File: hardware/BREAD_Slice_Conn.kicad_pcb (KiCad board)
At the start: 2 copper layers, 70 x 100 mm, 15 parts, among them J1 Conn_01x10_Female

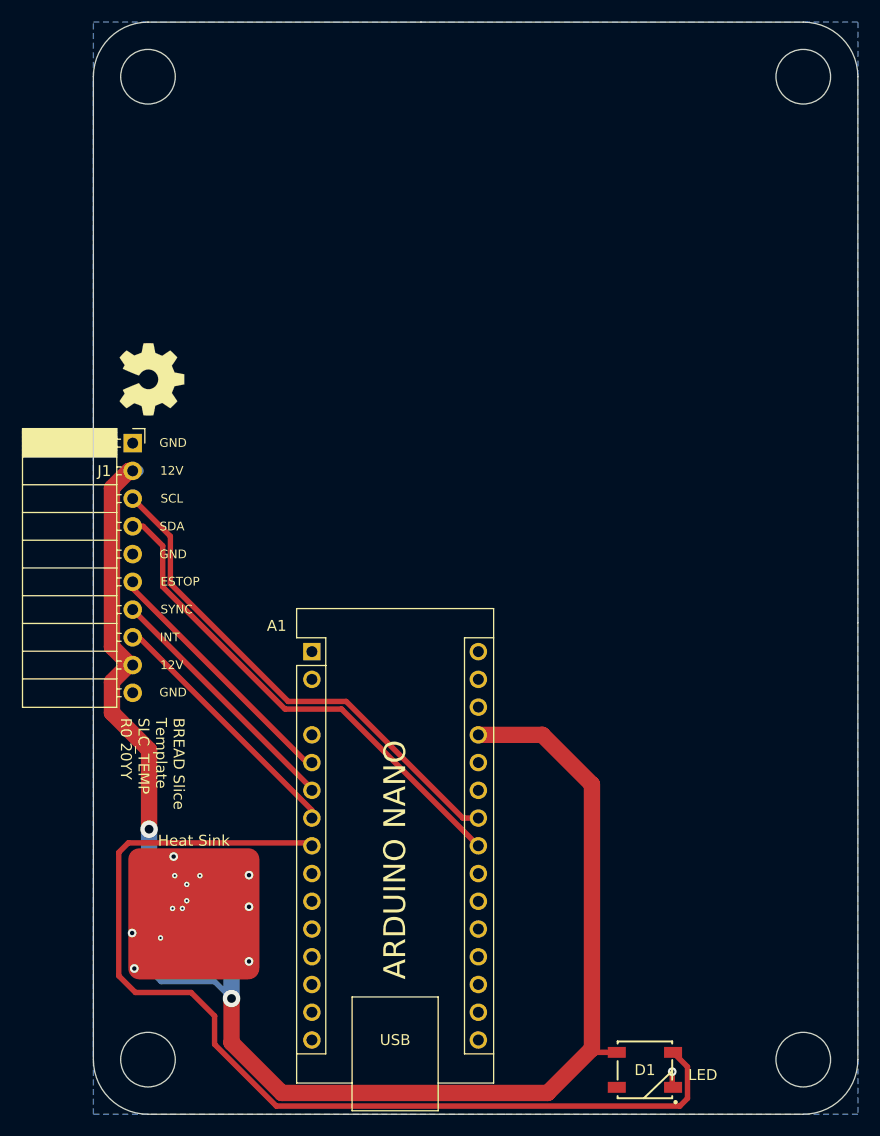
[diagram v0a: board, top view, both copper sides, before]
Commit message: updated template and added pcb vars for prototyping
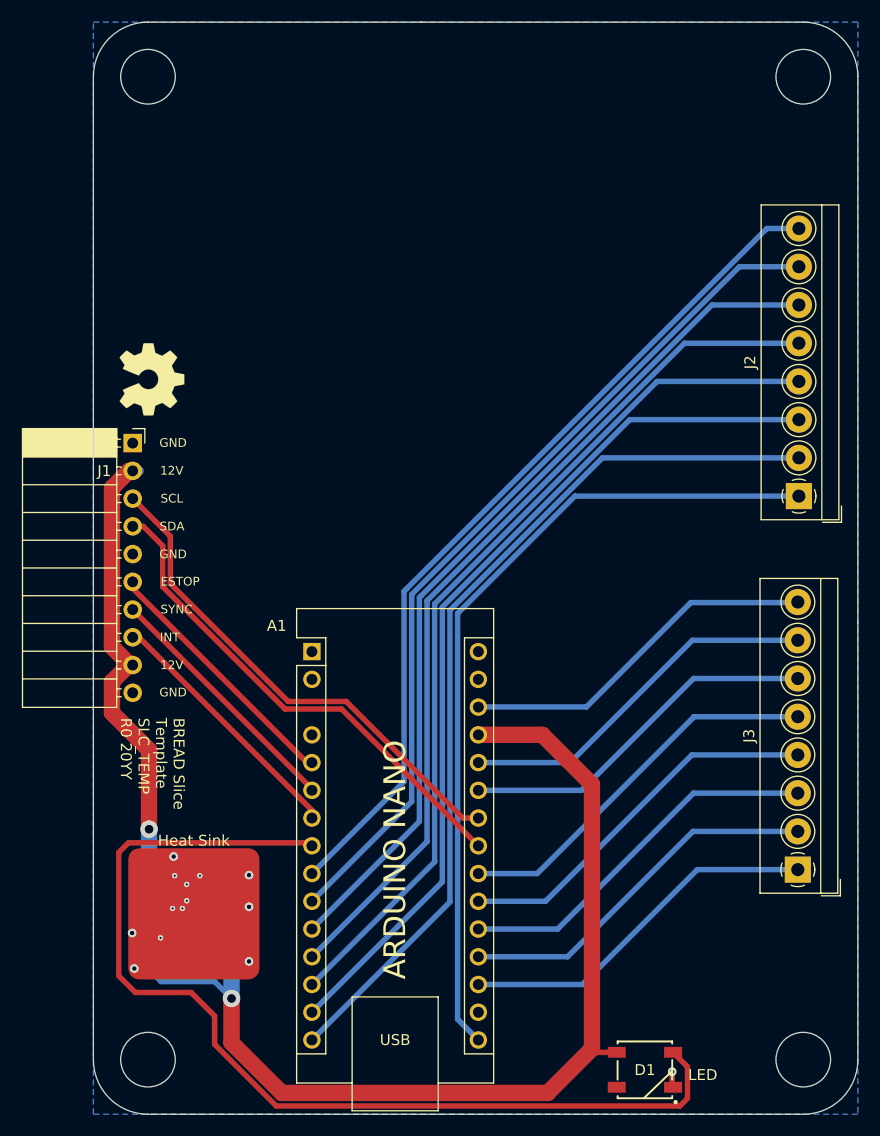
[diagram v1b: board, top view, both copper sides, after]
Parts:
- added J2: Conn_01x08, TerminalBlock_4Ucon:TerminalBlock_4Ucon_1x08_P3.50mm_Horizontal, F.Cu at (187.2, 83.2)
- added J3: Conn_01x08, TerminalBlock_4Ucon:TerminalBlock_4Ucon_1x08_P3.50mm_Horizontal, F.Cu at (187.1, 117.4)
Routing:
- net /D12: track 0.00 -> 82.5 mm
- net /D11: track 0.00 -> 81.8 mm
- net /D10: track 0.00 -> 81.3 mm
- net /D9: track 0.00 -> 80.8 mm
- net /D8: track 0.00 -> 80.3 mm
- net /D7: track 0.00 -> 79.8 mm
- net /D6: track 0.00 -> 79.3 mm
- net /D13: track 0.00 -> 75.5 mm
- net /A3: track 0.00 -> 35.2 mm
- net /A2: track 0.00 -> 34.8 mm
- net /A1: track 0.00 -> 34.4 mm
- net /A0: track 0.00 -> 34.0 mm
- net /A7: track 0.00 -> 33.9 mm
- net /AREF: track 0.00 -> 33.6 mm
- net /A6: track 0.00 -> 33.5 mm
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
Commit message: removed old silk
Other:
- board text added: "BREAD Slice Template: -> Conn SLC_TEMP R2 04-2025"
- board text removed: "5V I2C Connector"
- board text removed: "BREAD Slice Template SLC_TEMP R0 20YY"
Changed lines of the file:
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@@
 		(attr smd)
 		(fp_text user "Heat Sink"
-			(at 0 -6.7 0)
+			(at -1.275 6.7 0)
 			(unlocked yes)
 			(layer "F.SilkS")
@@
 		)
 	)
-	(gr_text "5V I2C \nConnector"
-		(at 150.22 129.24 0)
-		(layer "B.SilkS")
-		(effects
-			(font
-				(size 1 1)
-				(thickness 0.15)
-			)
-			(justify bottom mirror)
-		)
-	)
 	(gr_text "GND"
 		(at 129.89619 88.522 0)
@@
 		)
 	)
-	(gr_text "BREAD Slice\nTemplate\nSLC_TEMP\nR0 20YY"
+	(gr_text "BREAD Slice\nTemplate:\n-> Conn\nSLC_TEMP\nR2 04-2025"
 		(at 128 103.5 270)
 		(layer "F.SilkS")
